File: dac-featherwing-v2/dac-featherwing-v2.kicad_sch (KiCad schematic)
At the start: 28 parts, among them J1 BOT, J2 TOP, J3 AudioJack4, J4 AudioJack4, U1 WM8731CLSEFL

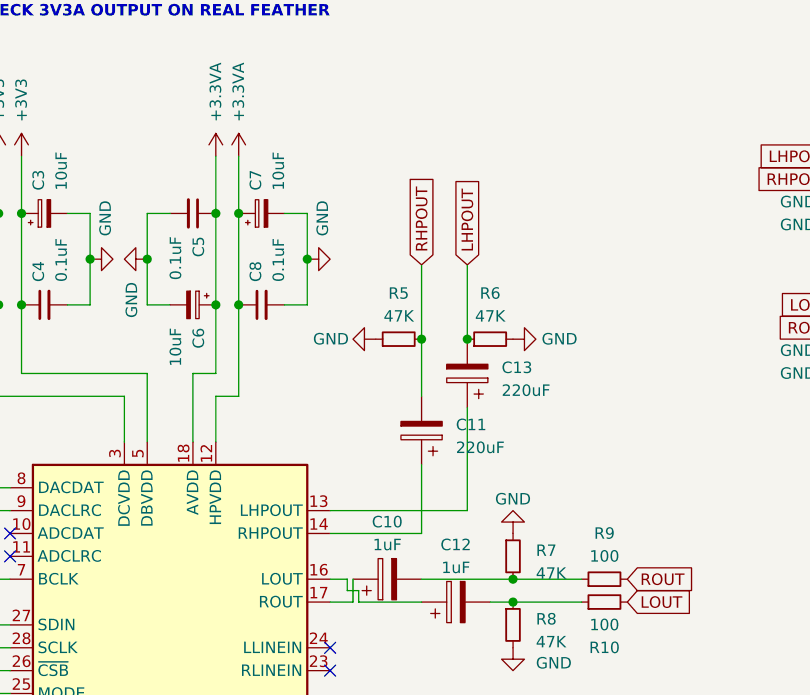
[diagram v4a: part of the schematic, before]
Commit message: Redid routing to be much better
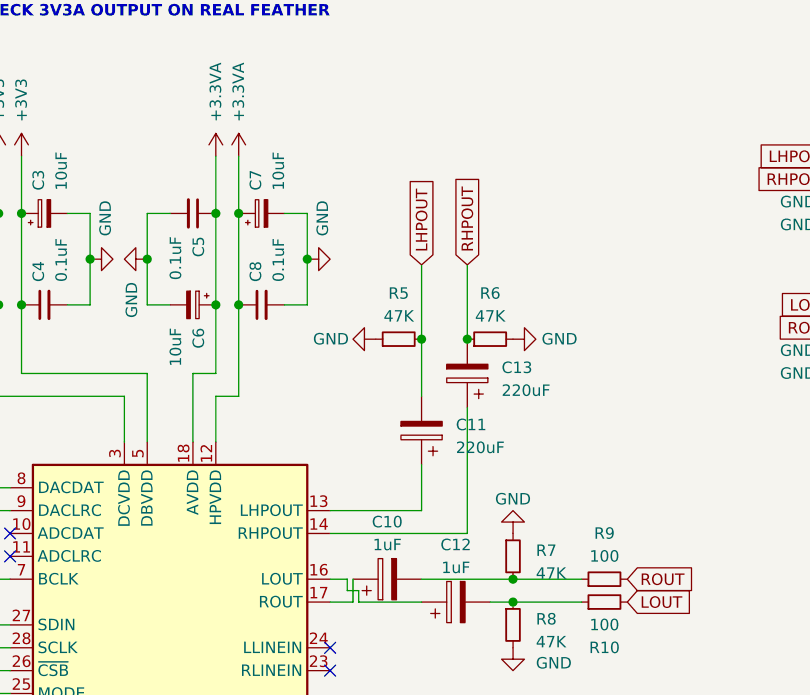
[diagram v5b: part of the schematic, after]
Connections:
- net LHPOUT: now also C11.2, R5.2; no longer C13.2, R6.1
- net RHPOUT: now also C13.2, R6.1; no longer C11.2, R5.2
- net at C11.1: now also U1.13 (LHPOUT); no longer U1.14 (RHPOUT)
- net at C13.1: now also U1.14 (RHPOUT); no longer U1.13 (LHPOUT)
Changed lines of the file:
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@@
     (stroke (width 0) (type solid) (color 0 0 0 0))
   )
-  (wire (pts (xy 157.48 96.52) (xy 172.72 96.52))
+  (wire (pts (xy 157.48 96.52) (xy 167.64 96.52))
     (stroke (width 0) (type solid) (color 0 0 0 0))
   )
-  (wire (pts (xy 157.48 99.06) (xy 167.64 99.06))
+  (wire (pts (xy 157.48 99.06) (xy 172.72 99.06))
     (stroke (width 0) (type solid) (color 0 0 0 0))
   )
@@
     (stroke (width 0) (type solid) (color 0 0 0 0))
   )
-  (wire (pts (xy 167.64 91.44) (xy 167.64 99.06))
+  (wire (pts (xy 167.64 91.44) (xy 167.64 96.52))
     (stroke (width 0) (type solid) (color 0 0 0 0))
   )
@@
     (stroke (width 0) (type solid) (color 0 0 0 0))
   )
-  (wire (pts (xy 172.72 96.52) (xy 172.72 85.09))
+  (wire (pts (xy 172.72 85.09) (xy 172.72 99.06))
     (stroke (width 0) (type solid) (color 0 0 0 0))
   )
@@
     )
   )
-  (global_label "RHPOUT" (shape input) (at 167.64 69.215 90) (fields_autoplaced)
+  (global_label "LHPOUT" (shape input) (at 167.64 69.215 90) (fields_autoplaced)
     (effects (font (size 1.27 1.27)) (justify left))
-    (property "Intersheet References" "${INTERSHEET_REFS}" (id 0) (at 167.5606 59.3029 90)
+    (property "Intersheet References" "${INTERSHEET_REFS}" (id 0) (at 167.5606 59.5448 90)
       (effects (font (size 1.27 1.27)) (justify left) hide)
     )
   )
-  (global_label "LHPOUT" (shape input) (at 172.72 69.215 90) (fields_autoplaced)
+  (global_label "RHPOUT" (shape input) (at 172.72 69.215 90) (fields_autoplaced)
     (effects (font (size 1.27 1.27)) (justify left))
-    (property "Intersheet References" "${INTERSHEET_REFS}" (id 0) (at 172.6406 59.5448 90)
+    (property "Intersheet References" "${INTERSHEET_REFS}" (id 0) (at 172.6406 59.3029 90)
       (effects (font (size 1.27 1.27)) (justify left) hide)
     )

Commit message: DACV2 Complete. Ordered. Checked other files.
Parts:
- added JP1: 3V3A SRC, Jumper:SolderJumper-3_P2.0mm_Open_TrianglePad1.0x1.5mm_NumberLabels, symbol Jumper:SolderJumper_3_Open
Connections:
- net +3.3VA: now also JP1.2 (C); no longer J1.1 (Pin_1)
- net +3V3: now also JP1.1 (A)
- new net +3.3VDAC: J1.1 (Pin_1), JP1.3 (B)
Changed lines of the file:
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@@
     (effects (font (size 1.27 1.27) (thickness 0.254) bold) (justify left bottom))
   )
-  (text "TODO CHECK 3V3A OUTPUT ON REAL FEATHER" (at 111.76 41.91 0)
+  (text "TODO CHECK 3V3A OUTPUT ON REAL FEATHER" (at 111.76 30.48 0)
     (effects (font (size 1.27 1.27) (thickness 0.254) bold) (justify left bottom))
   )
@@
     (pin "1")
   )
-  (symbol (lib_id "power:+3.3VA") (at 71.12 60.96 90) (unit 1)
-    (in_bom yes) (on_board yes)
-    (property "Reference" "#PWR0102" (id 0) (at 74.93 60.96 0)
-      (effects (font (size 1.27 1.27)) hide)
-    )
-    (property "Value" "+3.3VA" (id 1) (at 67.31 60.96 90)
-      (effects (font (size 1.27 1.27)) (justify left))
+  (symbol (lib_id "power:+3.3VDAC") (at 71.12 60.96 90) (unit 1)
+    (in_bom yes) (on_board yes)
+    (property "Reference" "#PWR0102" (id 0) (at 72.39 57.15 0)
+      (effects (font (size 1.27 1.27)) hide)
+    )
+    (property "Value" "+3.3VDAC" (id 1) (at 59.055 60.9599 90)
+      (effects (font (size 1.27 1.27)) (justify right))
     )
     (property "Footprint" "" (id 2) (at 71.12 60.96 0)
@@
     )
     (property "Datasheet" "" (id 3) (at 123.19 57.15 0)
+      (effects (font (size 1.27 1.27)) hide)
+    )
+    (pin "1")
+  )
+  (symbol (lib_id "power:+3V3") (at 130.175 38.735 90) (unit 1)
+    (in_bom yes) (on_board yes)
+    (property "Reference" "#PWR0128" (id 0) (at 133.985 38.735 0)
+      (effects (font (size 1.27 1.27)) hide)
+    )
+    (property "Value" "+3V3" (id 1) (at 126.365 38.735 90)
+      (effects (font (size 1.27 1.27)) (justify left))
+    )
+    (property "Footprint" "" (id 2) (at 130.175 38.735 0)
+      (effects (font (size 1.27 1.27)) hide)
+    )
+    (property "Datasheet" "" (id 3) (at 130.175 38.735 0)
+      (effects (font (size 1.27 1.27)) hide)
+    )
+    (pin "1")
+  )
+  (symbol (lib_id "power:+3.3VA") (at 135.255 42.545 180) (unit 1)
+    (in_bom yes) (on_board yes)
+    (property "Reference" "#PWR0127" (id 0) (at 135.255 38.735 0)
+      (effects (font (size 1.27 1.27)) hide)
+    )
+    (property "Value" "+3.3VA" (id 1) (at 135.255 46.355 90)
+      (effects (font (size 1.27 1.27)) (justify left))
+    )
+    (property "Footprint" "" (id 2) (at 135.255 42.545 0)
+      (effects (font (size 1.27 1.27)) hide)
+    )
+    (property "Datasheet" "" (id 3) (at 135.255 42.545 0)
+      (effects (font (size 1.27 1.27)) hide)
+    )
+    (pin "1")
+  )
+  (symbol (lib_id "power:+3.3VDAC") (at 140.335 38.735 270) (unit 1)
+    (in_bom yes) (on_board yes)
+    (property "Reference" "#PWR0129" (id 0) (at 139.065 42.545 0)
+      (effects (font (size 1.27 1.27)) hide)
+    )
+    (property "Value" "+3.3VDAC" (id 1) (at 143.51 38.7349 90)
+      (effects (font (size 1.27 1.27)) (justify left))
+    )
+    (property "Footprint" "" (id 2) (at 140.335 38.735 0)
+      (effects (font (size 1.27 1.27)) hide)
+    )
+    (property "Datasheet" "" (id 3) (at 140.335 38.735 0)
       (effects (font (size 1.27 1.27)) hide)
     )
@@
     (pin "1")
     (pin "2")
+  )
+  (symbol (lib_id "Jumper:SolderJumper_3_Open") (at 135.255 38.735 0) (unit 1)
+    (in_bom yes) (on_board yes) (fields_autoplaced)
+    (property "Reference" "JP1" (id 0) (at 135.255 34.29 0))
+    (property "Value" "3V3A SRC" (id 1) (at 135.255 36.83 0))
+    (property "Footprint" "Jumper:SolderJumper-3_P2.0mm_Open_TrianglePad1.0x1.5mm_NumberLabels" (id 2) (at 135.255 38.735 0)
+      (effects (font (size 1.27 1.27)) hide)
+    )
+    (property "Datasheet" "~" (id 3) (at 135.255 38.735 0)
+      (effects (font (size 1.27 1.27)) hide)
+    )
+    (pin "1")
+    (pin "2")
+    (pin "3")
   )
   (symbol (lib_id "Connector:AudioJack4") (at 219.71 62.23 180) (unit 1)
@@
       (reference "#PWR0101") (unit 1) (value "+BATT") (footprint "")
     )
-    (path "/6b110fa0-3b02-46ef-b2ef-9d8195915570"
-      (reference "#PWR0102") (unit 1) (value "+3.3VA") (footprint "")
+    (path "/df20a122-cb93-4bdd-83e5-acfe841321af"
+      (reference "#PWR0102") (unit 1) (value "+3.3VDAC") (footprint "")
     )
     (path "/e206efb0-d487-4d83-8dd9-f0b7f705335f"
@@
       (reference "#PWR0126") (unit 1) (value "GND") (footprint "")
     )
+    (path "/d21a4a37-a498-4307-88c3-76e775aabff5"
+      (reference "#PWR0127") (unit 1) (value "+3.3VA") (footprint "")
+    )
+    (path "/cd2ce752-5b9c-4a0d-9b1a-1adf3438bb29"
+      (reference "#PWR0128") (unit 1) (value "+3V3") (footprint "")
+    )
+    (path "/14569996-2dfe-405f-ae84-dae814bda2f8"
+      (reference "#PWR0129") (unit 1) (value "+3.3VDAC") (footprint "")
+    )
     (path "/1ca37de6-2e96-420b-a373-4aae964d1d81"
       (reference "C1") (unit 1) (value "0.1uF") (footprint "Capacitor_SMD:C_0805_2012Metric_Pad1.18x1.45mm_HandSolder")
@@
       (reference "J4") (unit 1) (value "AudioJack4") (footprint "Footprints:Lumberg 1503 20 VP3")
     )
+    (path "/db191cc5-ba8f-4bbc-8147-6b3c7bfbdd47"
+      (reference "JP1") (unit 1) (value "3V3A SRC") (footprint "Jumper:SolderJumper-3_P2.0mm_Open_TrianglePad1.0x1.5mm_NumberLabels")
+    )
     (path "/1abb9351-ad36-4fb2-b13b-3ae130f82d03"
